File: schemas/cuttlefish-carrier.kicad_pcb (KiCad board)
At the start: 2 copper layers, 87.5 x 63 mm, 15 parts

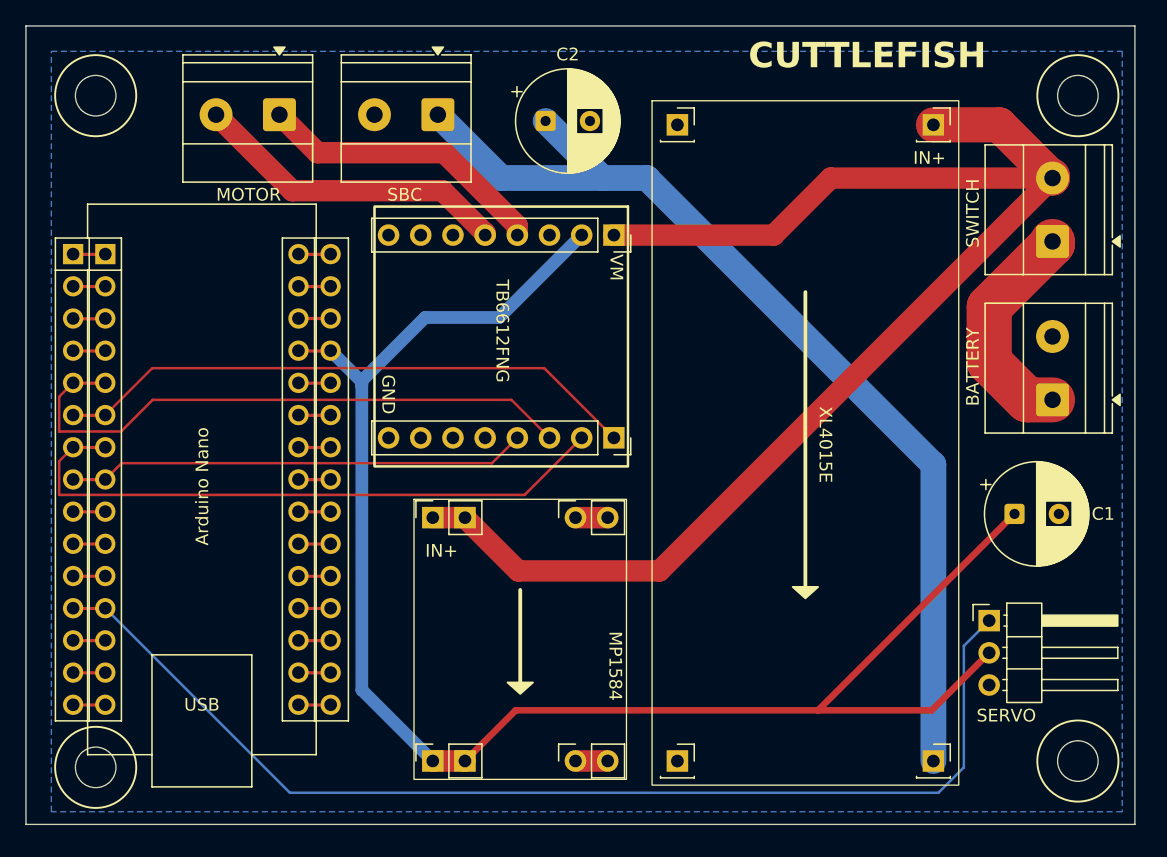
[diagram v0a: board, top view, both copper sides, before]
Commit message: pcb: fix hole positions and padding
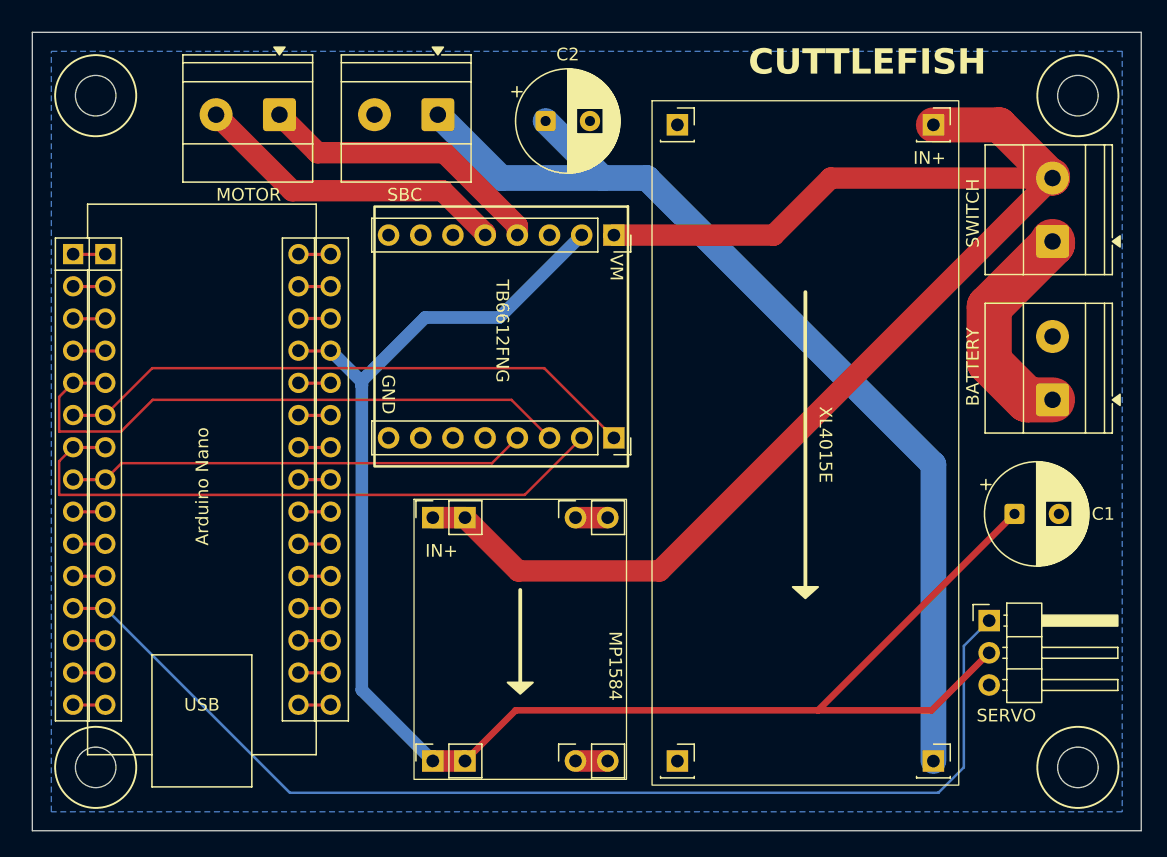
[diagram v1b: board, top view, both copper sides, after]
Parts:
- moved REF** 0.50 mm to (131.0, 106.5)
